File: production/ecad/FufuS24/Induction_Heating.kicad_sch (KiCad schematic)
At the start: 21 parts, among them IC1 FOD3150, J1 Conn_01x02, M1 MLX90614ESF-AAA-000-TU, U3 STGP8NC60KD, U8 AD8561

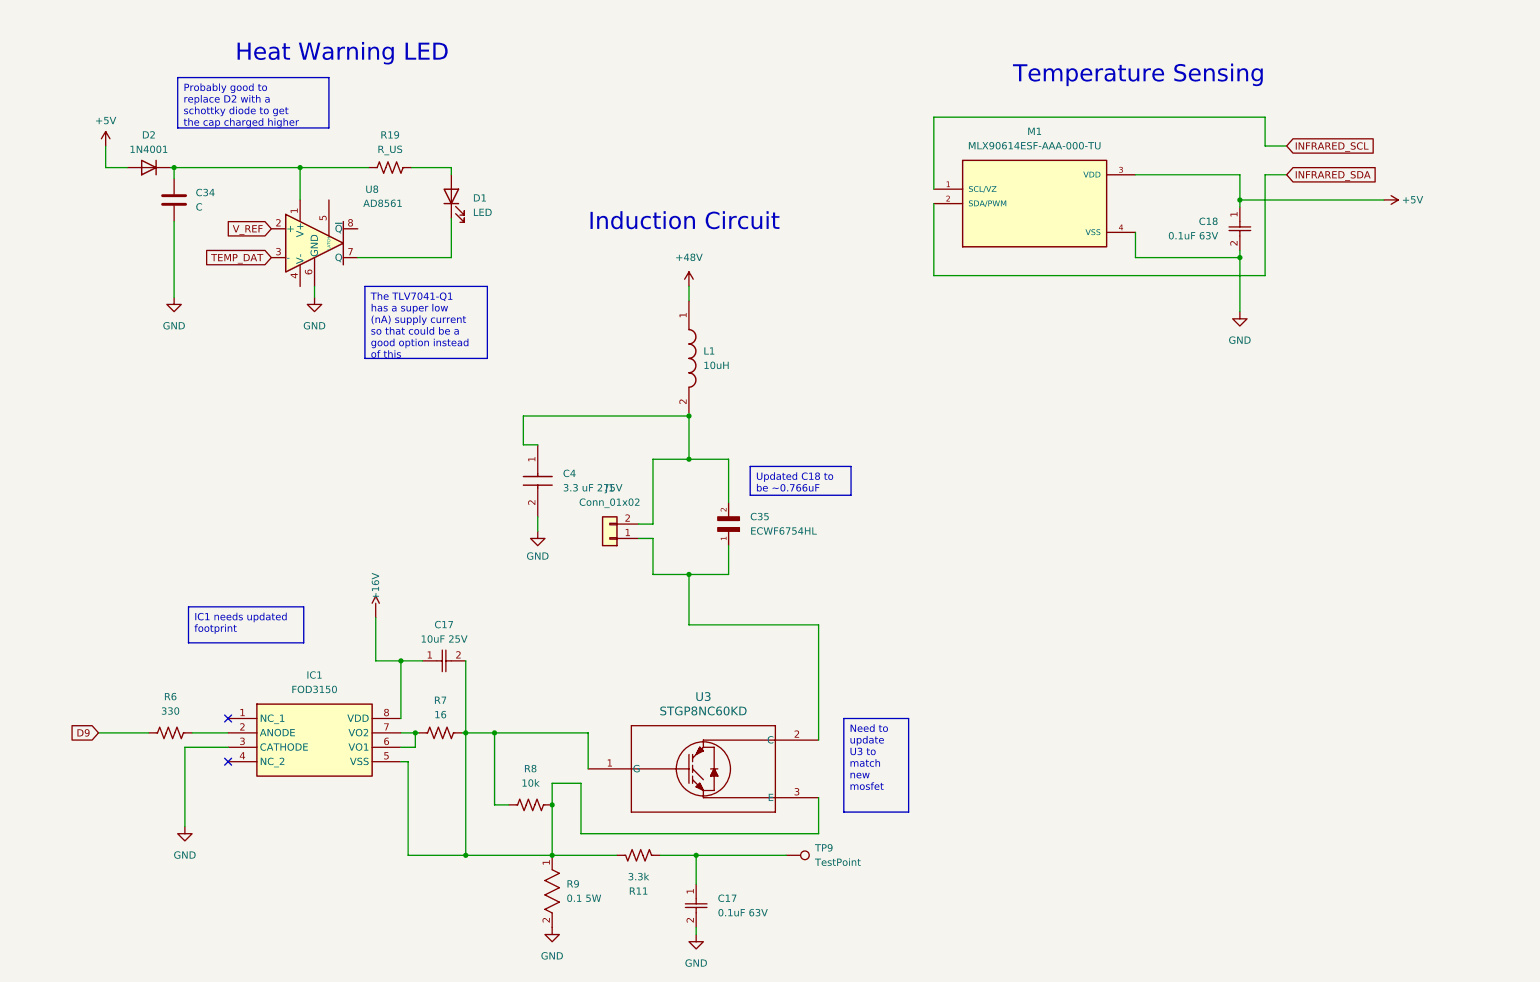
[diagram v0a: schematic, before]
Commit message: added LEDs
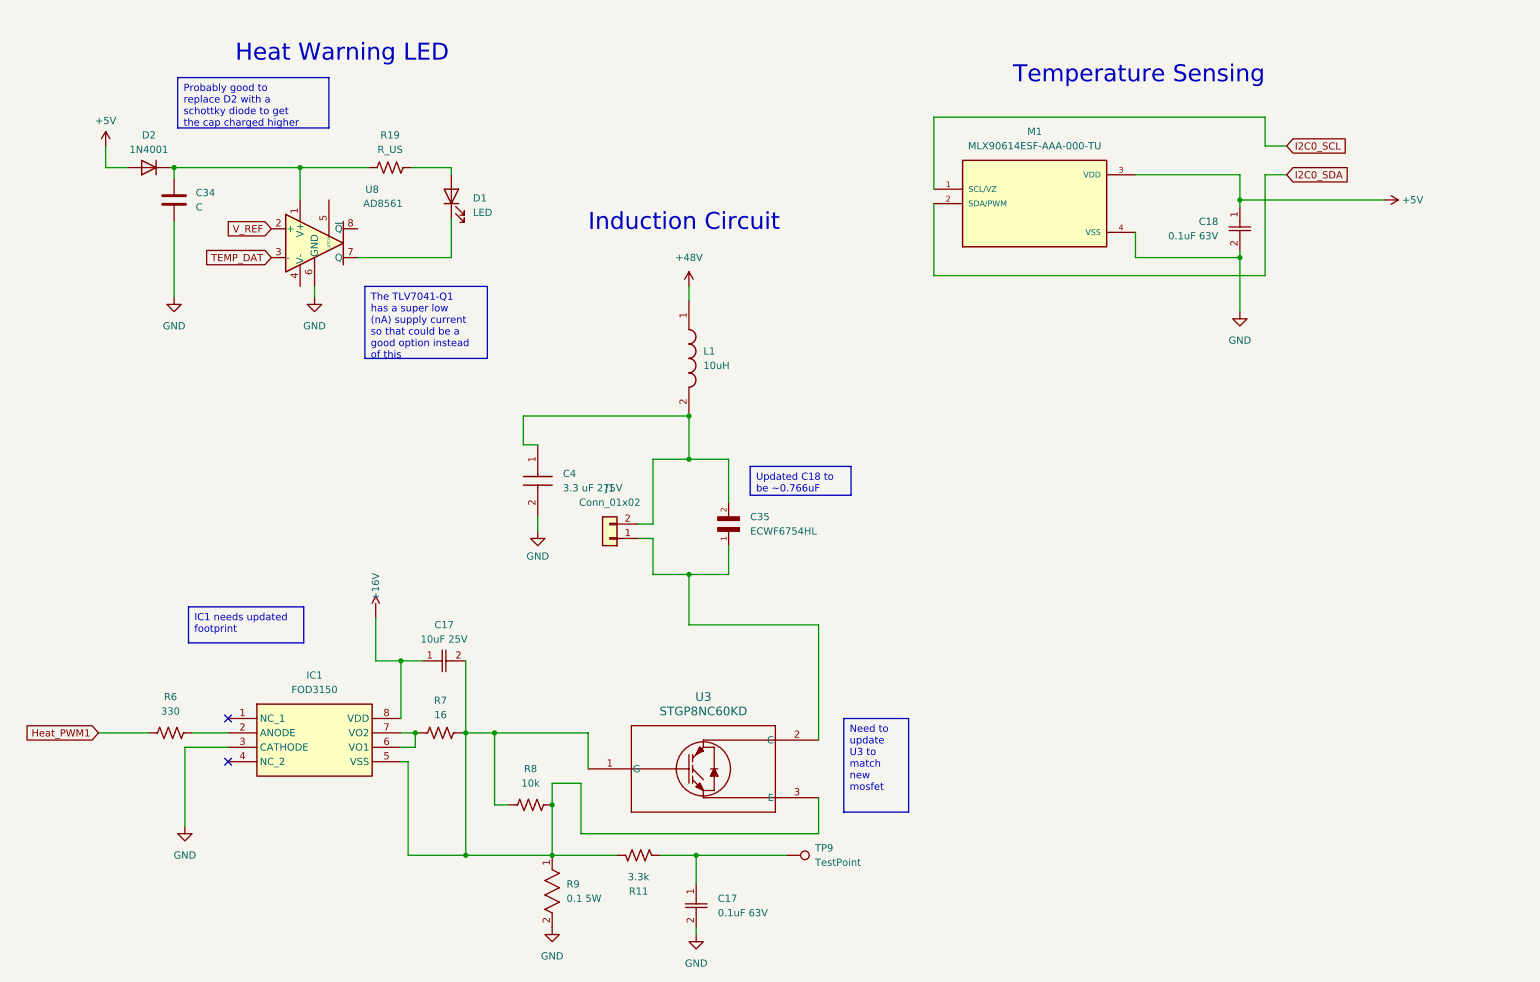
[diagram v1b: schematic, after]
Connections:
- net D9 renamed Heat_PWM1
- net INFRARED_SCL renamed I2C0_SCL
- net INFRARED_SDA renamed I2C0_SDA
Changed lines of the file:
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@@
     (effects (font (size 3 3)) (justify left bottom))
   )
-  (global_label "D9" (shape input) (at 26.67 138.43 180) (fields_autoplaced)
+  (global_label "Heat_PWM1" (shape input) (at 26.67 138.43 180) (fields_autoplaced)
     (effects (font (size 1.27 1.27)) (justify right))
-    (property "Intersheetrefs" "${INTERSHEET_REFS}" (at 21.2053 138.43 0)
+    (property "Intersheetrefs" "${INTERSHEET_REFS}" (at 13.0411 138.43 0)
       (effects (font (size 1.27 1.27)) (justify right) hide)
     )
   )
-  (global_label "INFRARED_SDA" (shape input) (at 236.22 40.005 0) (fields_autoplaced)
+  (global_label "I2C0_SDA" (shape input) (at 236.22 40.005 0) (fields_autoplaced)
     (effects (font (size 1.27 1.27)) (justify left))
-    (property "Intersheetrefs" "${INTERSHEET_REFS}" (at 252.8124 40.005 0)
+    (property "Intersheetrefs" "${INTERSHEET_REFS}" (at 248.0347 40.005 0)
       (effects (font (size 1.27 1.27)) (justify left) hide)
     )
@@
     )
   )
-  (global_label "INFRARED_SCL" (shape input) (at 236.22 34.925 0) (fields_autoplaced)
+  (global_label "I2C0_SCL" (shape input) (at 236.22 34.925 0) (fields_autoplaced)
     (effects (font (size 1.27 1.27)) (justify left))
-    (property "Intersheetrefs" "${INTERSHEET_REFS}" (at 252.7519 34.925 0)
+    (property "Intersheetrefs" "${INTERSHEET_REFS}" (at 247.9742 34.925 0)
       (effects (font (size 1.27 1.27)) (justify left) hide)
     )

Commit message: Incorporated schematic review feedback
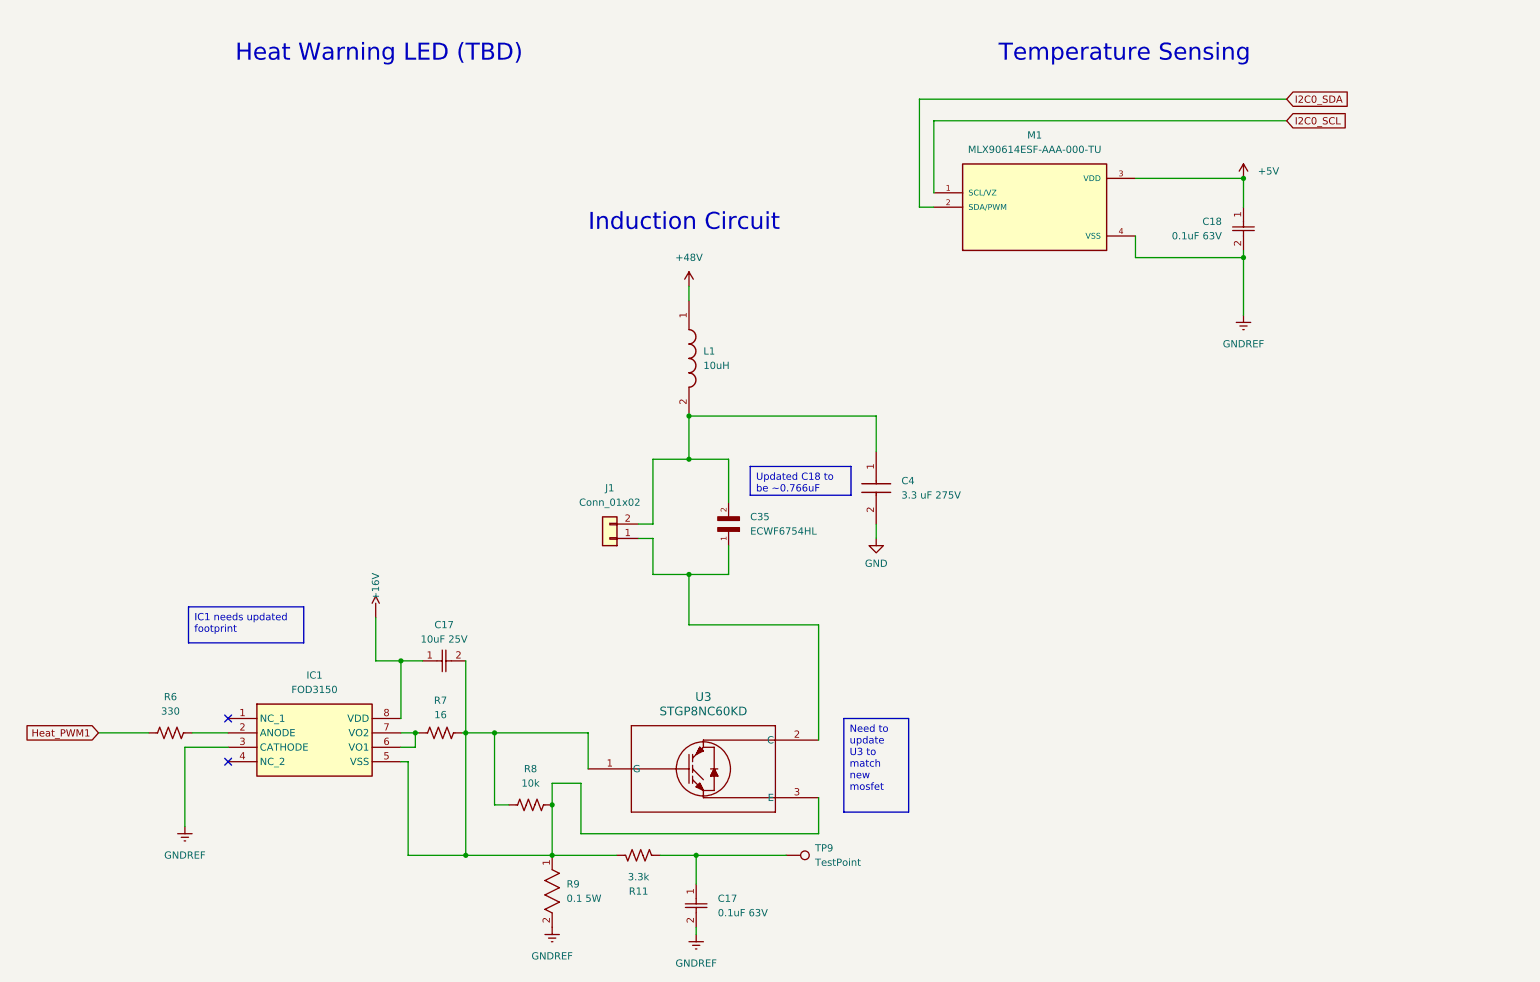
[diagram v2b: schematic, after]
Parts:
- removed C34: C, symbol Device:C
- removed D1: LED, symbol Device:LED
- removed D2: 1N4001, Diode_THT:D_DO-41_SOD81_P10.16mm_Horizontal, symbol Diode:1N4001
- removed R19: R_US, symbol Device:R_US
- removed U8: AD8561, symbol Comparator:AD8561
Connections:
- net GND: no longer C17.2, C18.2, IC1.3 (CATHODE), M1.4 (VSS), R9.2
- new net GNDREF: C17.2, C18.2, IC1.3 (CATHODE), M1.4 (VSS), R9.2
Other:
- note added: "Heat Warning LED (TBD)"
- note removed: "Heat Warning LED"
- moved on the sheet: C18, C4, M1

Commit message: cleaned up schematic
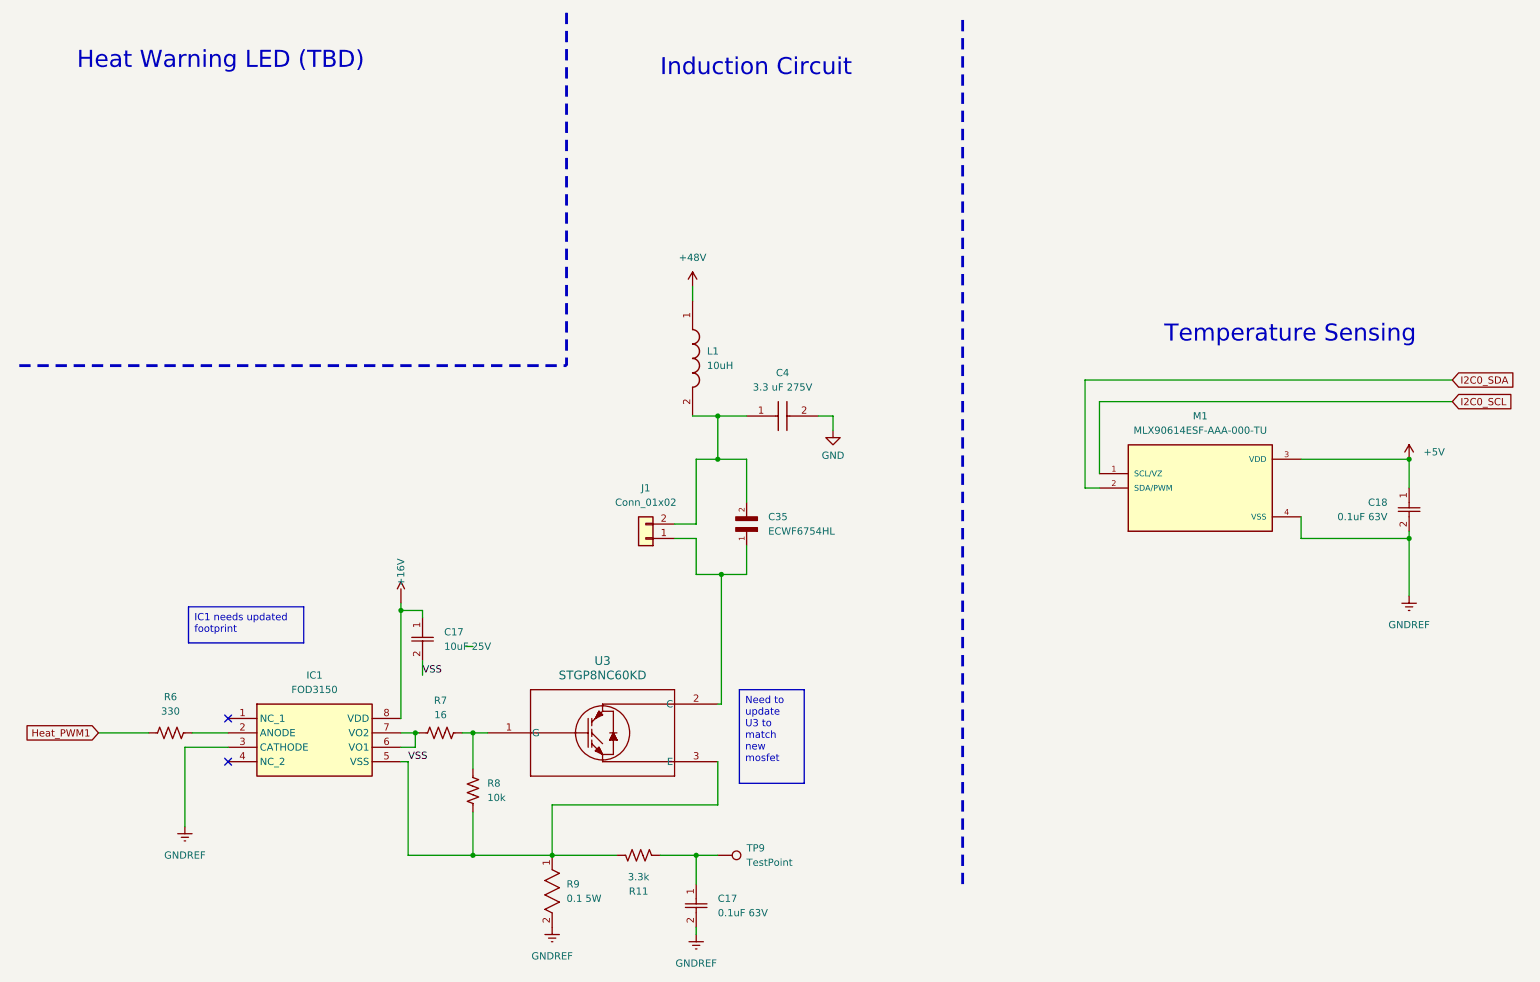
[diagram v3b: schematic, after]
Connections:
- net VSS: now reaches C17.2, IC1.5 (VSS), R11.1, R8.1, R9.1, U3.3 (E)
- net VSS: no longer R7.2, R8.2, U3.1 (G)
- new net: R7.2, R8.2, U3.1 (G)
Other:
- moved on the sheet: C17, C18, C35, C4, J1, L1, M1, TP9, U3

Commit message: Ethan Changes
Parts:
- removed IC1: FOD3150, FODfootprints:SMD8_9P91X6P86_ONS, symbol FOD3150:FOD3150
- removed U3: STGP8NC60KD, TO225P1040X460X1968-3(1):TO225P1040X460X1968-3, symbol STGP8NC60KD:STGP8NC60KD
- added U8: ~, symbol New_Library_0:FOD3150
- added U9: ~, symbol New_Library:IRFB4610PBF
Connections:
- net +16V: now also U8.8 (VDD)
- net GNDREF: now also U8.2 (ANODE)
- net VSS: now also U8.5 (VSS), U9.3 (S)
- net at R7.2, R8.2: now also U9.1 (G)
- net at C35.1, J1.1 (Pin_1): now also U9.2 (D)
- net at R6.2: now also U8.3 (CATHODE)
- net at R7.1: now also U8.6 (VO1), U8.7 (VO2)

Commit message: efan
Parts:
- added J14: 691137710002, CONN2_710002_WRE, symbol 2024-03-03_19-32-21:691137710002
- renumbered C17 to C49
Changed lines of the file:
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@@
+    )
+  )
+  (symbol (lib_id "2024-03-03_19-32-21:691137710002") (at 47.625 38.735 0) (unit 1)
+    (in_bom yes) (on_board yes) (dnp no) (fields_autoplaced)
+    (property "Reference" "J14" (at 62.23 38.735 0)
+      (effects (font (size 1.524 1.524)) (justify left))
+    )
+    (property "Value" "691137710002" (at 62.23 41.275 0)
+      (effects (font (size 1.524 1.524)) (justify left))
+    )
+    (property "Footprint" "CONN2_710002_WRE" (at 47.625 38.735 0)
+      (effects (font (size 1.27 1.27) italic) hide)
+    )
+    (property "Datasheet" "691137710002" (at 47.625 38.735 0)
+      (effects (font (size 1.27 1.27) italic) hide)
+    )
+    (pin "1")
+    (pin "2")
+    (instances
+      (project "FufuS24"
+        (path "/c4c3980b-c8c0-435e-abdc-bbed2349d7ac/57fb5dcd-e779-40d3-8741-57c7eee1ca58"
+          (reference "J14") (unit 1)
+        )
+      )
     )
   )
@@
   (symbol (lib_id "2023-11-09_20-51-41:860020772001") (at 132.08 165.1 270) (unit 1)
     (in_bom yes) (on_board yes) (dnp no) (fields_autoplaced)
-    (property "Reference" "C17" (at 135.89 167.64 90)
+    (property "Reference" "C49" (at 135.89 167.64 90)
       (effects (font (size 1.27 1.27)) (justify left))
     )
@@
       (project "FufuS24"
         (path "/c4c3980b-c8c0-435e-abdc-bbed2349d7ac/57fb5dcd-e779-40d3-8741-57c7eee1ca58"
-          (reference "C17") (unit 1)
-        )
-      )
+          (reference "C49") (unit 1)
+        )
+      )

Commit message: efan 2
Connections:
- net Temp_Light_Pos: now reaches J14.1
- net Temp_Light_Neg: now reaches J14.2
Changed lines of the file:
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@@
+    (stroke (width 0) (type default))
+  )
+  (wire (pts (xy 41.91 41.275) (xy 47.625 41.275))
     (stroke (width 0) (type default))
   )
@@
     (stroke (width 0) (type default))
   )
+  (wire (pts (xy 41.91 38.735) (xy 47.625 38.735))
+    (stroke (width 0) (type default))
+  )
   (wire (pts (xy 49.53 147.32) (xy 55.88 147.32))
     (stroke (width 0) (type default))
@@
     (effects (font (size 1.27 1.27)) (justify left bottom))
   )
+  (global_label "Temp_Light_Neg" (shape input) (at 41.91 41.275 180) (fields_autoplaced)
+    (effects (font (size 1.27 1.27)) (justify right))
+    (property "Intersheetrefs" "${INTERSHEET_REFS}" (at 23.8664 41.275 0)
+      (effects (font (size 1.27 1.27)) (justify right) hide)
+    )
+  )
   (global_label "Heat_PWM1" (shape input) (at 26.67 138.43 180) (fields_autoplaced)
     (effects (font (size 1.27 1.27)) (justify right))
@@
     )
   )
+  (global_label "Temp_Light_Pos" (shape input) (at 41.91 38.735 180) (fields_autoplaced)
+    (effects (font (size 1.27 1.27)) (justify right))
+    (property "Intersheetrefs" "${INTERSHEET_REFS}" (at 23.9874 38.735 0)
+      (effects (font (size 1.27 1.27)) (justify right) hide)
+    )
+  )

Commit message: efan 3
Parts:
- C17: footprint footprints:U1-E_NCH -> footprints:CAPC2012X94N
- C18, C49: footprint 8600footprint:CAP_WCAP-ATG5_05.0X11.0_WRE -> footprints:CAPC2012X94N
- C4: footprint KiCad:ECQUAAF335LD -> footprints:CAPC2012X94N
- J14: footprint CONN2_710002_WRE -> footprints:CONN2_710002_WRE
- R11, R6, R7, R8: footprint (none) -> footprints:RESC2012X60N
- R9: footprint SQPfootprints:RES_SQP500_22X9P5_YAG -> footprints:RESC2012X60N
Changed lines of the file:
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@@
       (effects (font (size 1.524 1.524)) (justify left))
     )
-    (property "Footprint" "CONN2_710002_WRE" (at 47.625 38.735 0)
+    (property "Footprint" "footprints:CONN2_710002_WRE" (at 47.625 38.735 0)
       (effects (font (size 1.27 1.27) italic) hide)
     )
@@
       (effects (font (size 1.27 1.27)))
     )
-    (property "Footprint" "" (at 122.174 161.036 90)
+    (property "Footprint" "footprints:RESC2012X60N" (at 122.174 161.036 90)
       (effects (font (size 1.27 1.27)) hide)
     )
@@
       (effects (font (size 1.27 1.27)) (justify left))
     )
-    (property "Footprint" "footprints:U1-E_NCH" (at 83.82 118.11 0)
+    (property "Footprint" "footprints:CAPC2012X94N" (at 83.82 118.11 0)
       (effects (font (size 1.27 1.27) italic) hide)
     )
@@
       (effects (font (size 1.27 1.27)) (justify left))
     )
-    (property "Footprint" "SQPfootprints:RES_SQP500_22X9P5_YAG" (at 106.68 160.02 0)
+    (property "Footprint" "footprints:RESC2012X60N" (at 106.68 160.02 0)
       (effects (font (size 1.27 1.27) italic) hide)
     )
@@
       (effects (font (size 1.27 1.27)) (justify left))
     )
-    (property "Footprint" "8600footprint:CAP_WCAP-ATG5_05.0X11.0_WRE" (at 132.08 165.1 0)
+    (property "Footprint" "footprints:CAPC2012X94N" (at 132.08 165.1 0)
       (effects (font (size 1.27 1.27) italic) hide)
     )
@@
       (effects (font (size 1.27 1.27)))
     )
-    (property "Footprint" "" (at 39.624 137.414 90)
+    (property "Footprint" "footprints:RESC2012X60N" (at 39.624 137.414 90)
       (effects (font (size 1.27 1.27)) hide)
     )
@@
       (effects (font (size 1.27 1.27)))
     )
-    (property "Footprint" "" (at 87.249 137.414 90)
+    (property "Footprint" "footprints:RESC2012X60N" (at 87.249 137.414 90)
       (effects (font (size 1.27 1.27)) hide)
     )
@@
       (effects (font (size 1.27 1.27)))
     )
-    (property "Footprint" "KiCad:ECQUAAF335LD" (at 149.86 178.74 0)
+    (property "Footprint" "footprints:CAPC2012X94N" (at 149.86 178.74 0)
       (effects (font (size 1.27 1.27)) (justify left top) hide)
     )
@@
       (effects (font (size 1.27 1.27)) (justify left))
     )
-    (property "Footprint" "8600footprint:CAP_WCAP-ATG5_05.0X11.0_WRE" (at 257.81 95.25 0)
+    (property "Footprint" "footprints:CAPC2012X94N" (at 257.81 95.25 0)
       (effects (font (size 1.27 1.27) italic) hide)
     )
@@
       (effects (font (size 1.27 1.27)) (justify right))
     )
-    (property "Footprint" "" (at 91.694 148.336 90)
-      (effects (font (size 1.27 1.27)) hide)
-    )
+    (property "Footprint" "footprints:RESC2012X60N" (at 91.694 148.336 90)
+      (effects (font (size 1.27 1.27)) hide)
+    )

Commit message: efan 5
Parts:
- J1: footprint B2B-XH-A_LF__SN_:JST_B2B-XH-A_LF__SN_ -> footprints:CON_5025840270_MOL
- TP9: footprint TestPoint:TestPoint_Pad_2.0x2.0mm -> footprints:TP_5014
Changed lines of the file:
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@@
       (effects (font (size 1.27 1.27)) (justify left))
     )
-    (property "Footprint" "TestPoint:TestPoint_Pad_2.0x2.0mm" (at 135.89 165.1 0)
+    (property "Footprint" "footprints:TP_5014" (at 135.89 165.1 0)
       (effects (font (size 1.27 1.27)) hide)
     )
@@
       (effects (font (size 1.27 1.27)))
     )
-    (property "Footprint" "B2B-XH-A_LF__SN_:JST_B2B-XH-A_LF__SN_" (at 123.19 104.14 0)
+    (property "Footprint" "footprints:CON_5025840270_MOL" (at 123.19 104.14 0)
       (effects (font (size 1.27 1.27)) hide)
     )
